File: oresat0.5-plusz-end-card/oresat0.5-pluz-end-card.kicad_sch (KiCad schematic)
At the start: 34 parts, among them J1 J-SAMTEC-TFM-120-01-L-D-RA, J2 Harwin M55-7101242R, J3 Harwin M55-7101242R, J4 Harwin M55-7101242R, J5 Harwin M55-7101242R, J6 Conn_Coaxial

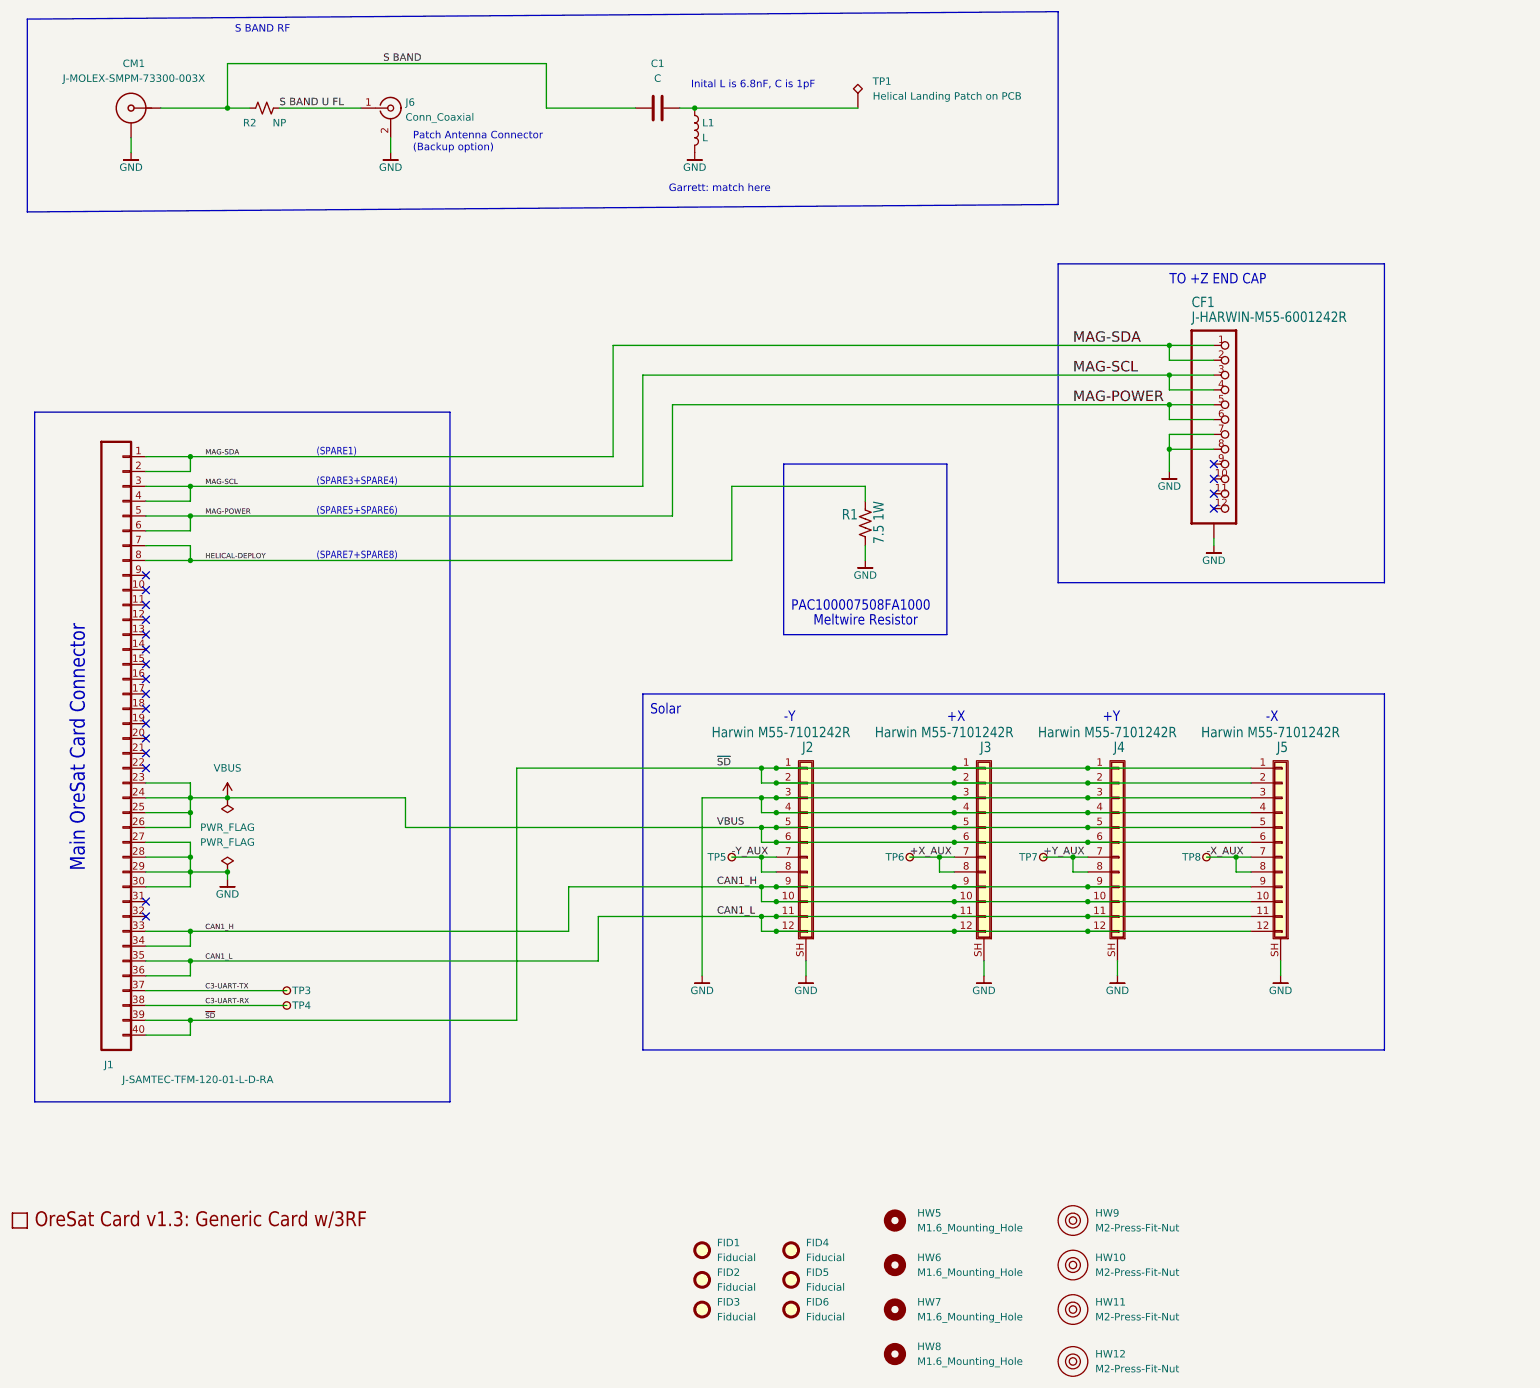
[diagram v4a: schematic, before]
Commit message: Updated OreSat 0.5 end card board outlines and mounting holes, and fixed KiCad library warnings
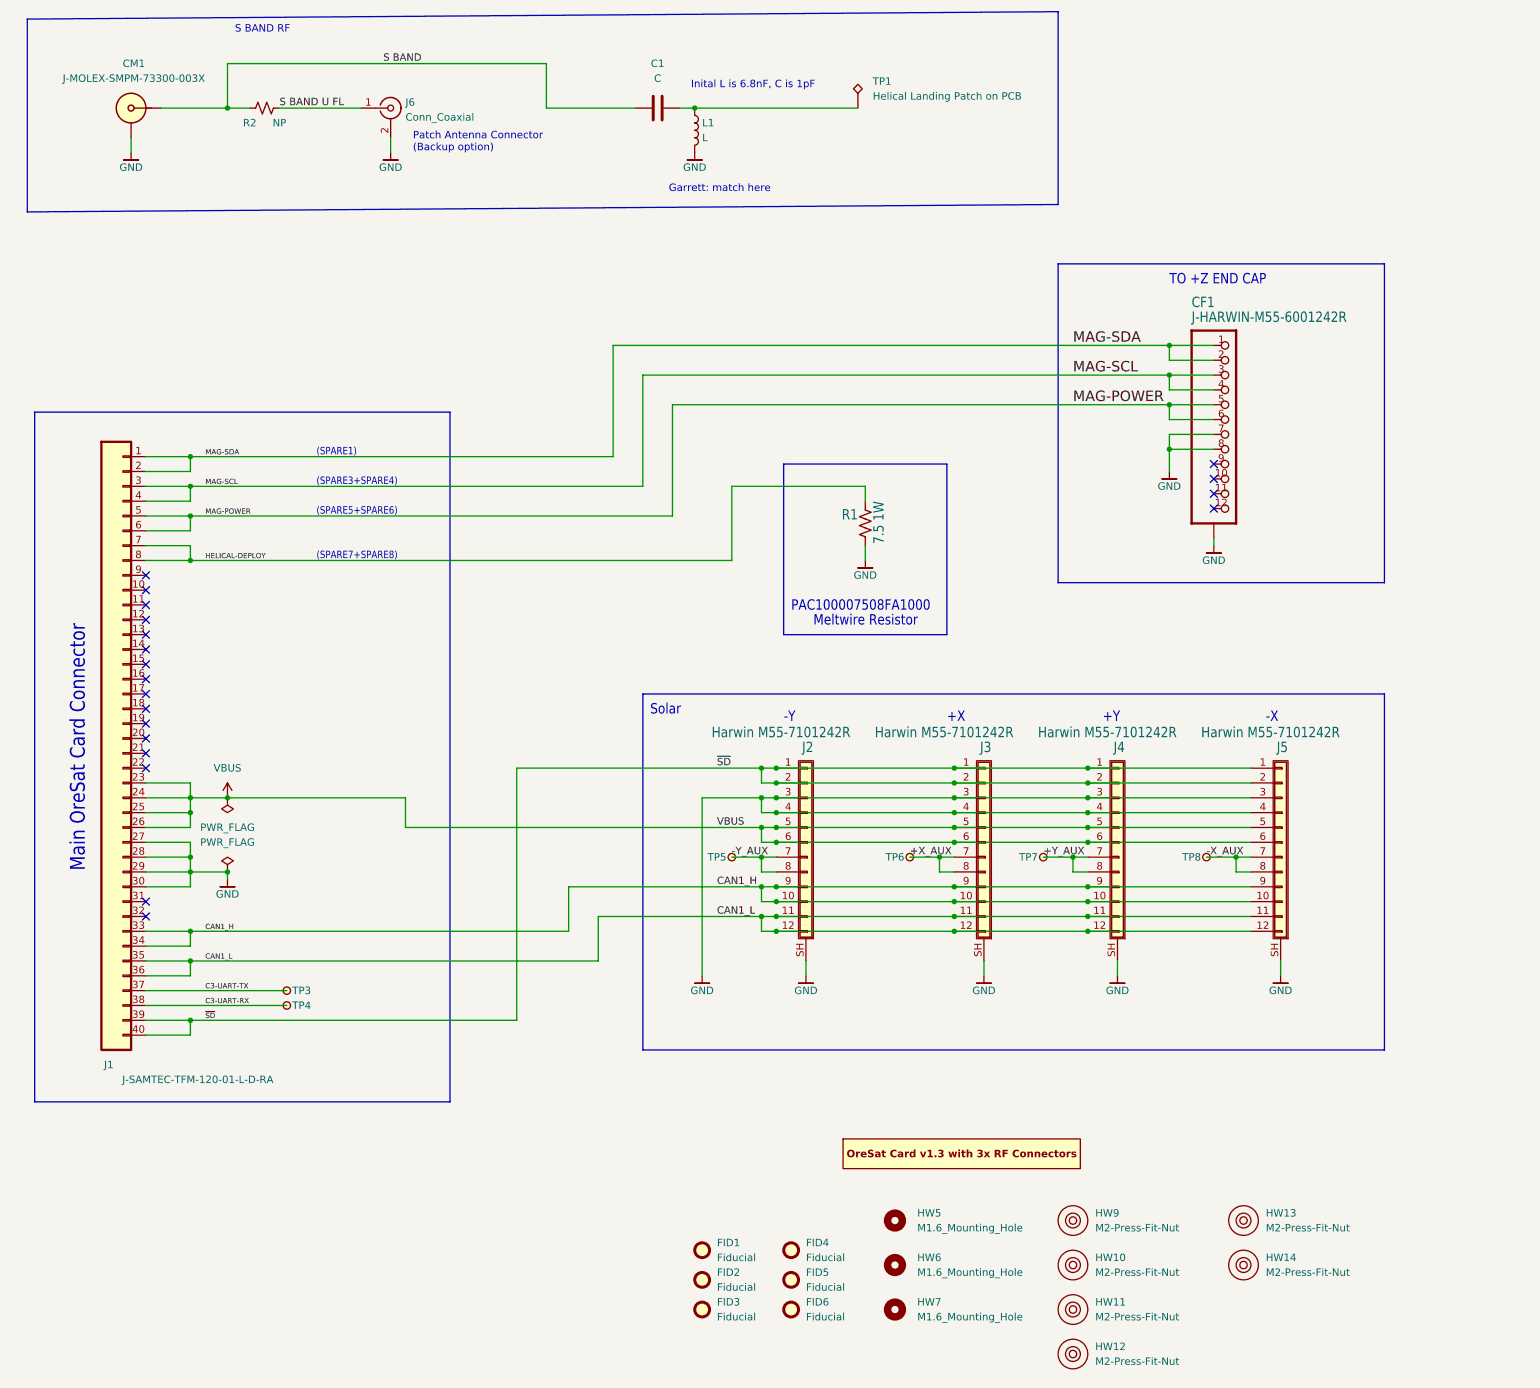
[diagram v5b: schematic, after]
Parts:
- removed HW7: M1.6_Mounting_Hole, oresat-misc:M1.6 Mounting Hole, symbol oresat-misc:M1.6_Mounting_Hole
- added HW13, HW14: M2-Press-Fit-Nut, oresat-misc:M2-Press-Fit-Nut, symbol oresat-misc:M2-Press-Fit-Nut
- CM1: footprint oresat-connectors:J-MOLEX-SMPM-073300-003X -> oresat-connectors:J-MOLEX-SMPM-073300-002X; symbol oresat-connectors:J-MOLEX-SMPM-73300-003X -> oresat-connectors:J-MOLEX-SMPM-73300-002X
- PCB1: footprint plusz-end-card-with-turnstile:ORESAT-CARD-V1.3-GENERIC-3RF -> oresat-pcbs:ORESAT-CARD-V1.3-3RF; symbol plusz-end-card-with-turnstile-eagle-import:ORESAT-CARD-V1.3-GENERIC-3RF -> oresat-pcbs:ORESAT-CARD-V1.3-3RF
- renumbered HW8 to HW7
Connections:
- net GND: now also CM1.SHLD; no longer CM1.GND (SHIELD3)
- net S BAND: now also CM1.SIG; no longer CM1.RF (CENTER)
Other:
- moved on the sheet: HW12, HW7

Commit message: Updated +Z end card
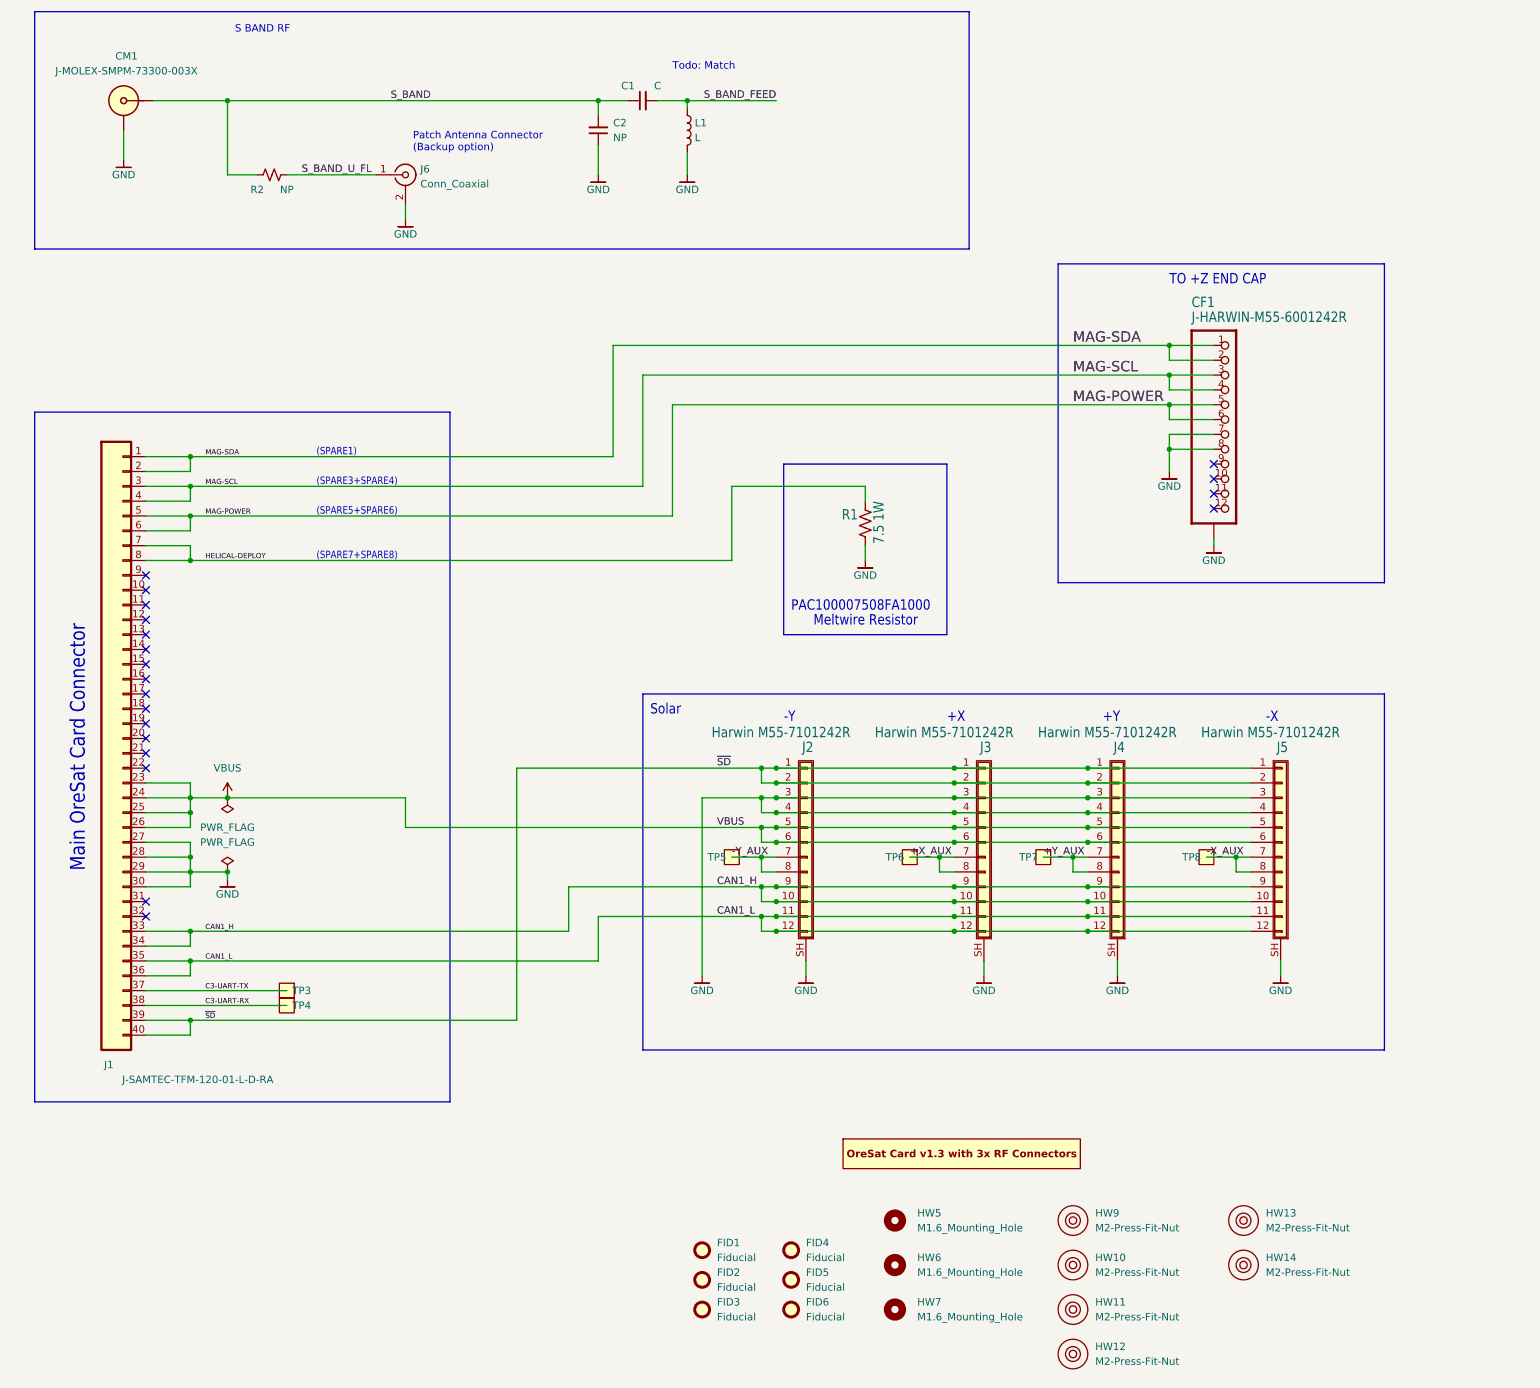
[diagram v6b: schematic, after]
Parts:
- removed TP1: Helical Landing Patch on PCB, TestPoint:TestPoint_Pad_2.5x2.5mm, symbol Connector:TestPoint_Alt
- added C2: NP, Capacitor_SMD:C_0402_1005Metric, symbol Device:C_Small
- C1: symbol Device:C -> Device:C_Small
- TP3, TP4, TP5, TP6, TP7, TP8: footprint oresat-misc:TestPoint-MinTH -> oresat-misc:TestPoint-0.75mm-th; symbol oresat-misc:TestPoint-MinTH -> oresat-misc:Test-Point-0.75mm-th
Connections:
- net GND: now also C2.1
- net S_BAND_FEED: now reaches C1.2, L1.1
- net S BAND renamed S_BAND
- net S_BAND: now also C2.2
- net S BAND U FL renamed S_BAND_U_FL
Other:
- note added: "Todo: Match"
- note removed: "Garrett: match here"
- note removed: "Inital L is 6.8nF, C is 1pF"
- moved on the sheet: C1, CM1, J6, L1, R2

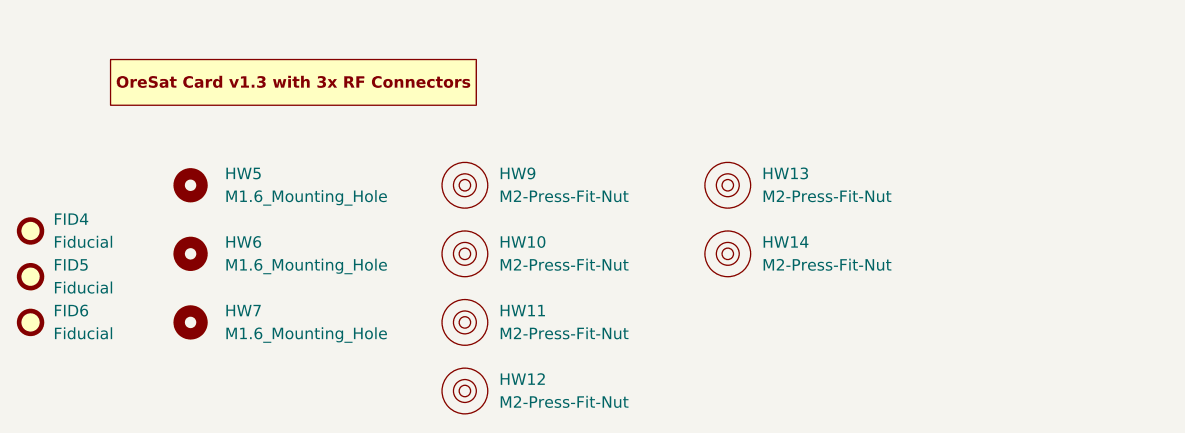
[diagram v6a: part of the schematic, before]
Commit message: Updated +Z end card mounting holes
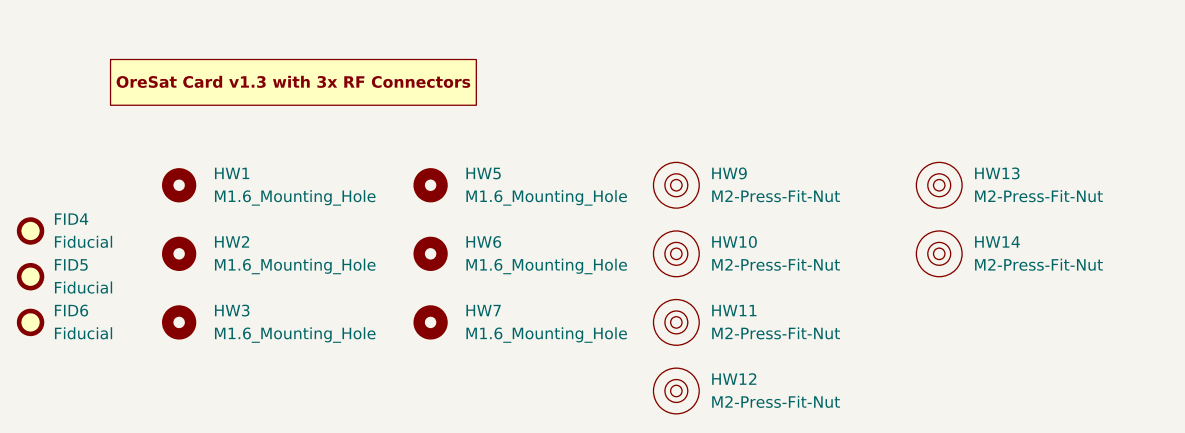
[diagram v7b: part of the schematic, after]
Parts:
- added HW1, HW2, HW3: M1.6_Mounting_Hole, oresat-misc:M1.6 Mounting Hole, symbol oresat-misc:M1.6_Mounting_Hole
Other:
- moved on the sheet: HW10, HW11, HW12, HW13, HW14, HW5, HW6, HW7, HW9
